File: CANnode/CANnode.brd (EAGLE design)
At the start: 57.9 x 57.7 mm, 247 parts, among them IC1 ISO1050DUB, IC2 ISO1050DUB, Q1 FDV302P, Q3 FDV302P, U1 LM324PW, U10 FT2232HL, U11 93LC56C-I/SN, U2 TPS70445_PWP_24, U3 LM324PW, U4 LM324PW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

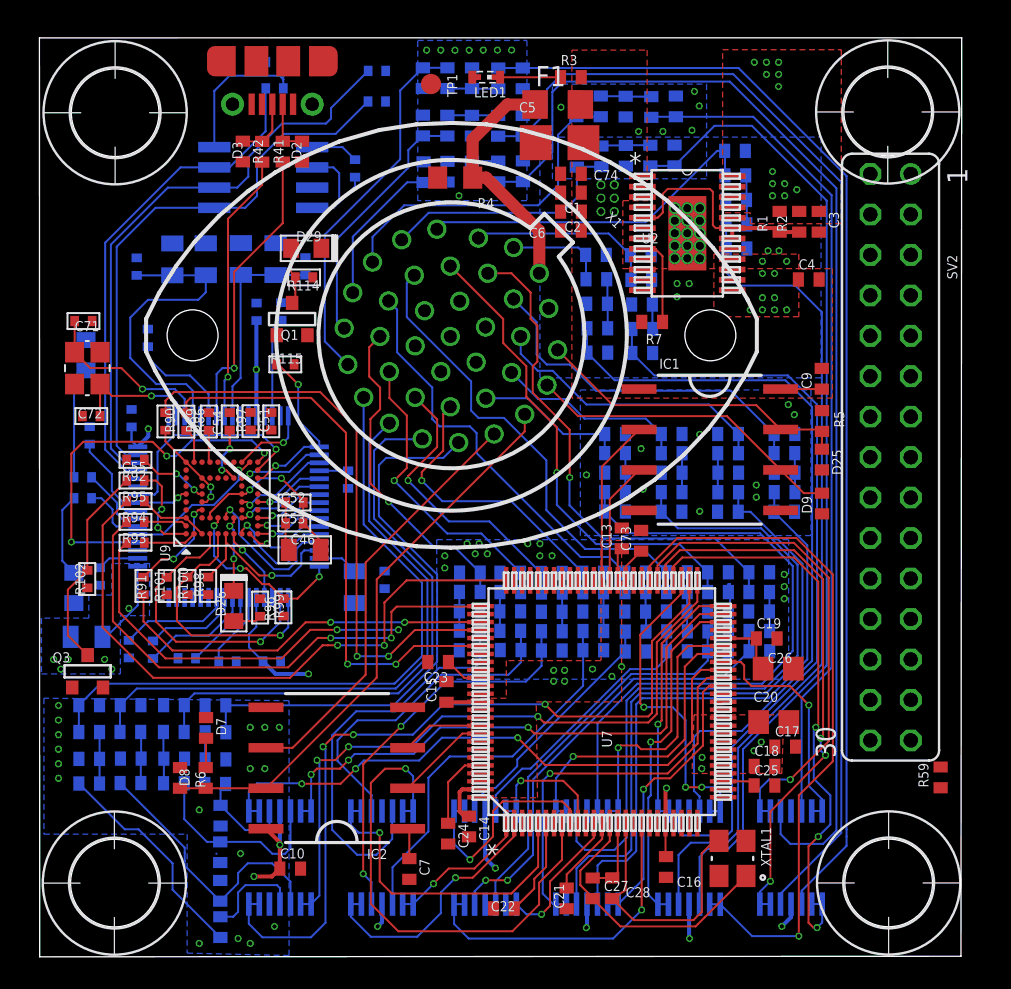
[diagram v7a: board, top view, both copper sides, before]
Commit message: Finished grounding bottom layer. Started routing +3V3
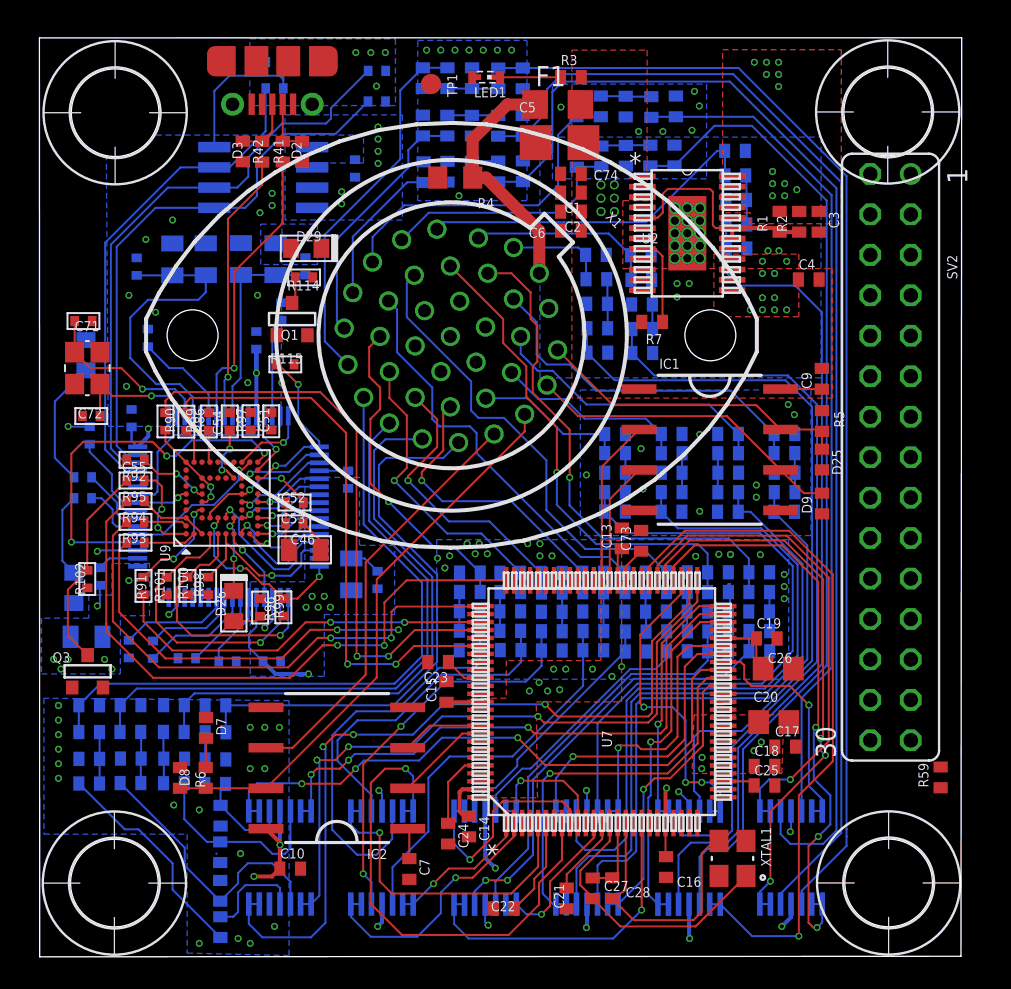
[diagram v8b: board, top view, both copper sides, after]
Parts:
- moved C61 1.79 mm to (21.6, 51.1)
- moved C57 0.83 mm to (27.5, 36.4)
- moved C65 0.44 mm to (29.2, 36.1)
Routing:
- net GND: track 12.4 -> 24.4 mm, vias 61 -> 95
- net +3V3: track 72.3 -> 64.2 mm, vias 16 -> 26
- net +1V8: track 25.8 -> 20.3 mm
- net N$43: track 7.02 -> 8.02 mm
- net D6_IN: track 30.2 -> 30.9 mm
- net A4_BUFFERED: track 36.3 -> 36.9 mm
- net D7_IN: track 32.1 -> 32.6 mm
- net A5_BUFFERED: track 34.9 -> 35.4 mm
- added copper zone on layer 16, net +3V3
